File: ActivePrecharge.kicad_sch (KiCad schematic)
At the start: 34 parts, among them Con1 LED, J1 Conn_01x03, J2 Conn_01x02, J3 Conn_01x02, Q1 IRLML0030, U1 NCP785AH50T1G, U2 NCP785AH50T1G, U3 TLV9301xDCK, U4 TCMT1106

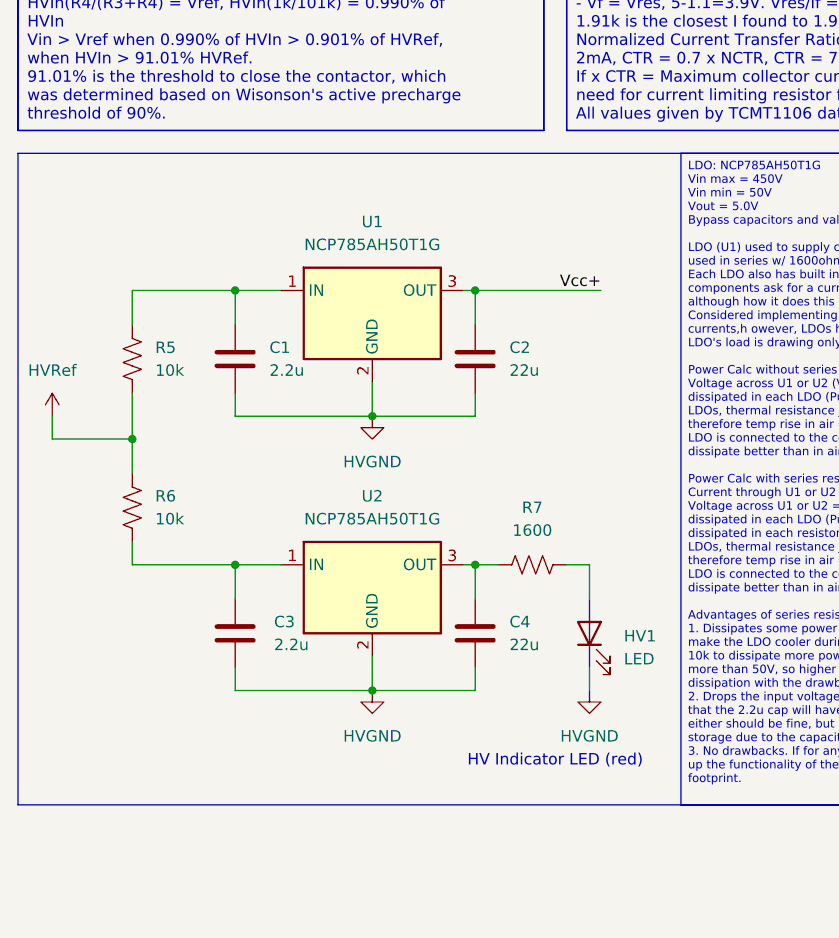
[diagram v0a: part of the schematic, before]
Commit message: 11/2 fixed incorrect footprint and symbol
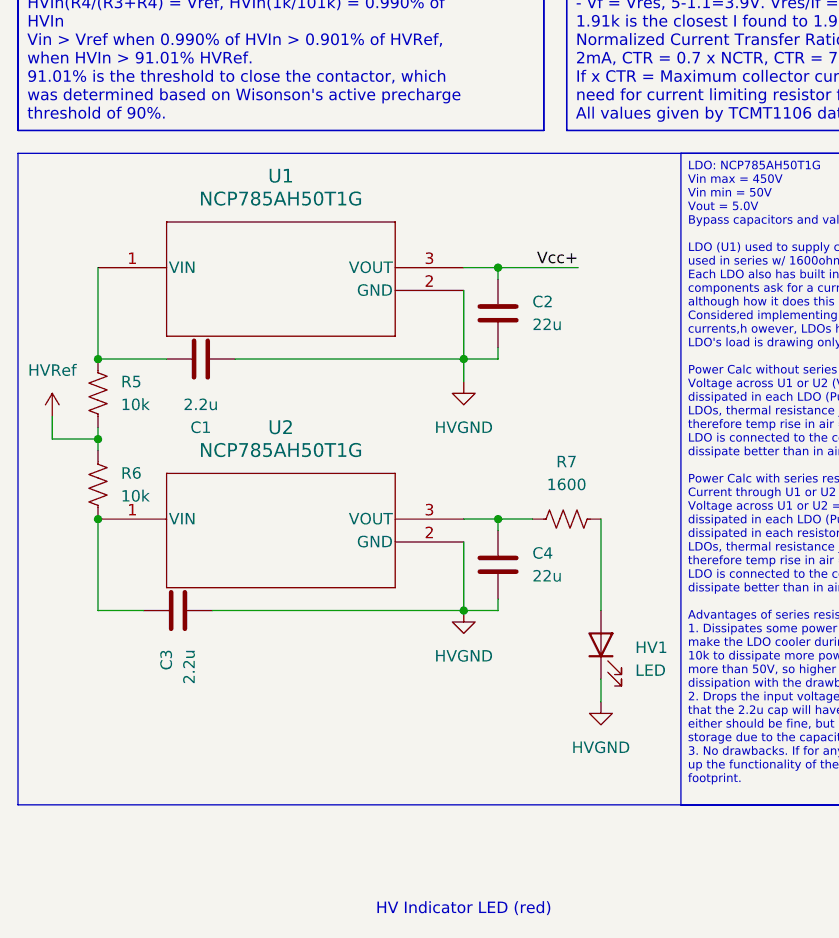
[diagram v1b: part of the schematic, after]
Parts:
- removed U1, U2: NCP785AH50T1G, Active-PrechargeLib:SOT-89-3_2P7X4P7_ONS, symbol Regulator_Linear:LT1963AxST-3.3
- added U1, U2: NCP785AH50T1G, Active-PrechargeLib:SOT-89-3_2P7X4P7_ONS, symbol NCP785:NCP785AH50T1G
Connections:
- net HVGND: now also C2.1, C4.1, U1.2 (GND), U2.2 (GND); no longer C2.2, C4.2
- net Vcc+: now also C2.2, U1.3 (VOUT); no longer C2.1
- net at C3.1, R6.1: now also U2.1 (VIN)
- net at R7.1: now also C4.2, U2.3 (VOUT); no longer C4.1
- net at C1.1, R5.2: now also U1.1 (VIN)
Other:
- moved on the sheet: C1, C2, C3, C4, HV1, R5, R6, R7

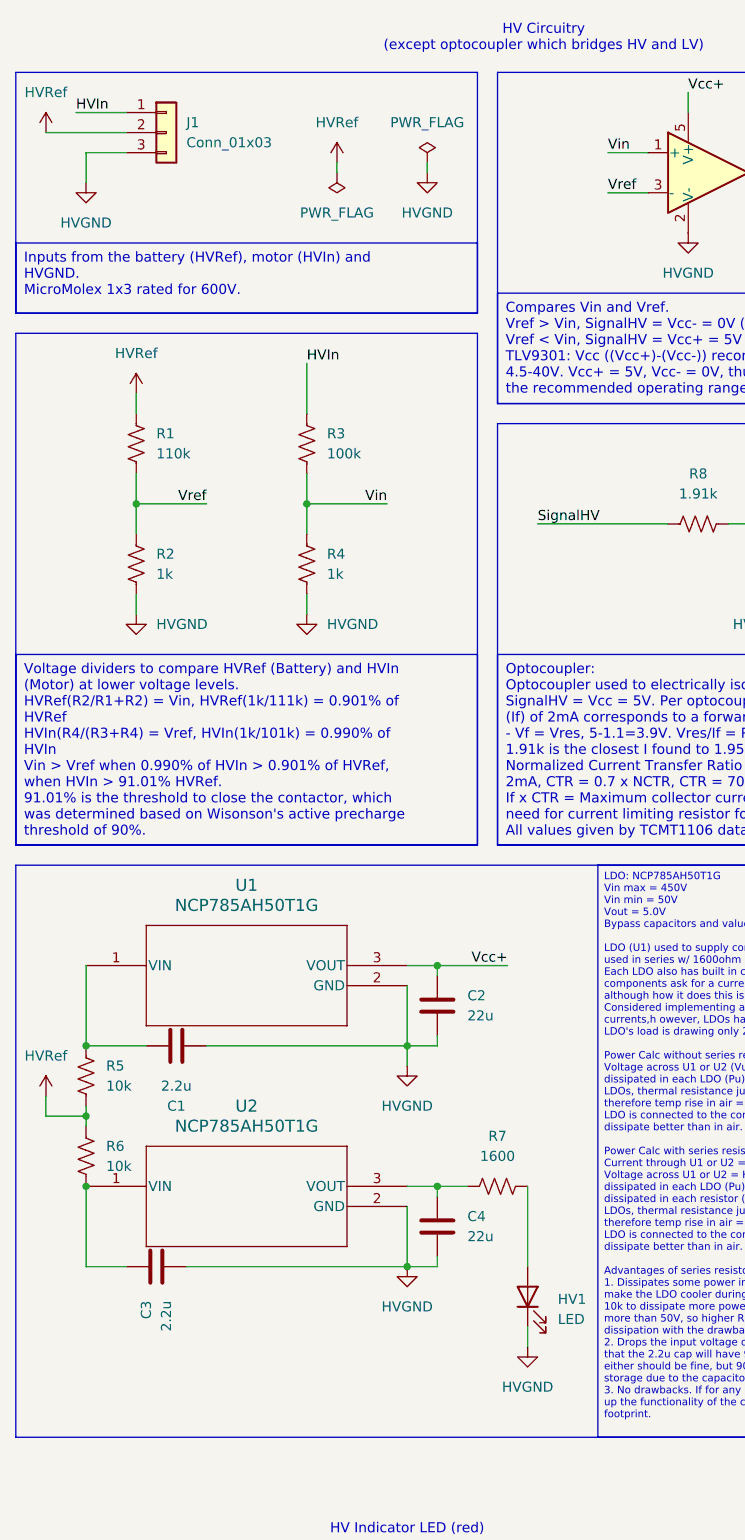
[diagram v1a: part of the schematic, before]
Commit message: adjusted HVGND position to be more centralized, added backplane traces and vias to route HVGND up to somewhat isolated top region, routed R1, R3 top plane traces on the back
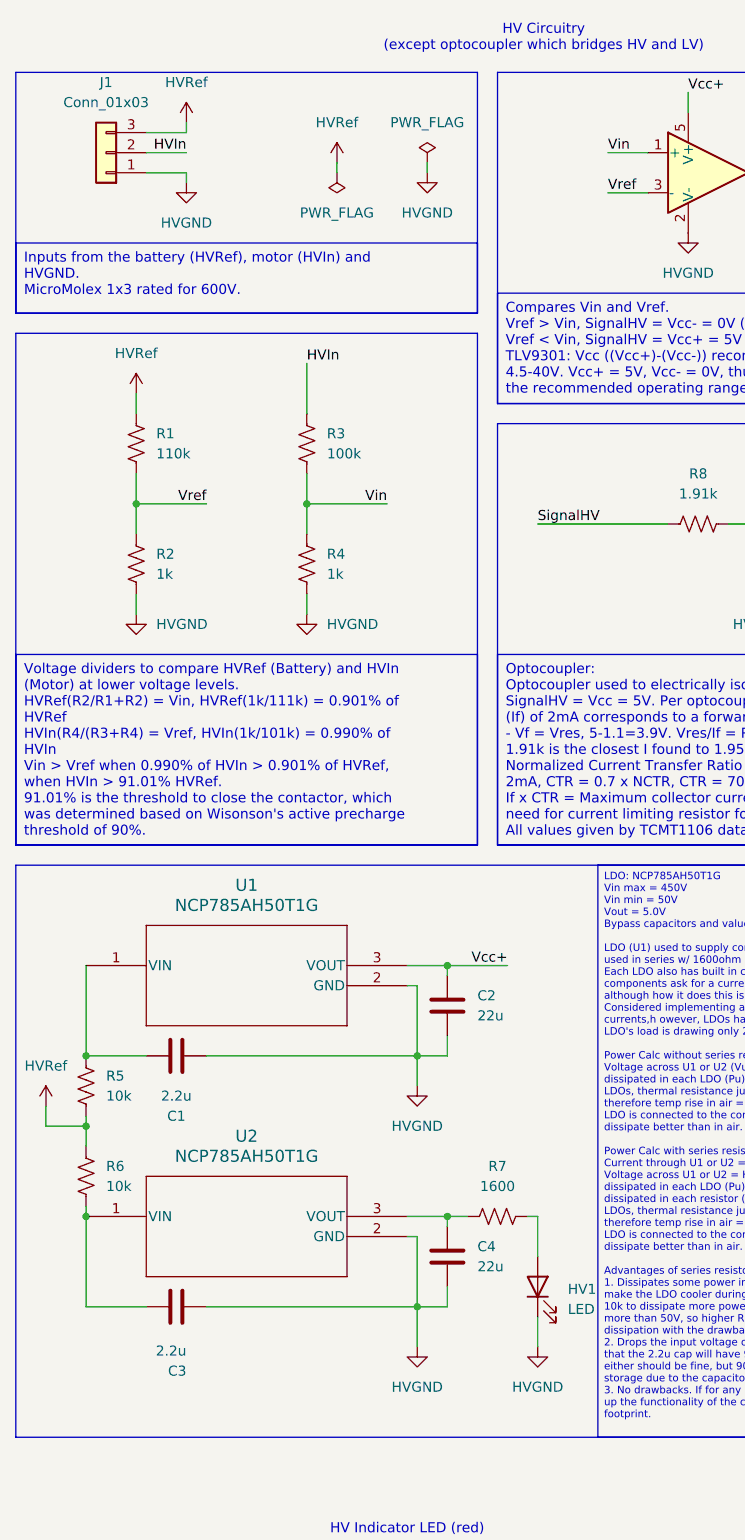
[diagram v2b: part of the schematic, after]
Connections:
- net HVGND: now also J1.1 (Pin_1); no longer J1.3 (Pin_3)
- net HVIn: now also J1.2 (Pin_2); no longer J1.1 (Pin_1)
- net HVRef: now also J1.3 (Pin_3); no longer J1.2 (Pin_2)
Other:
- moved on the sheet: C1, C2, C3, C4, HV1, J1, R5, R6, R7, U2

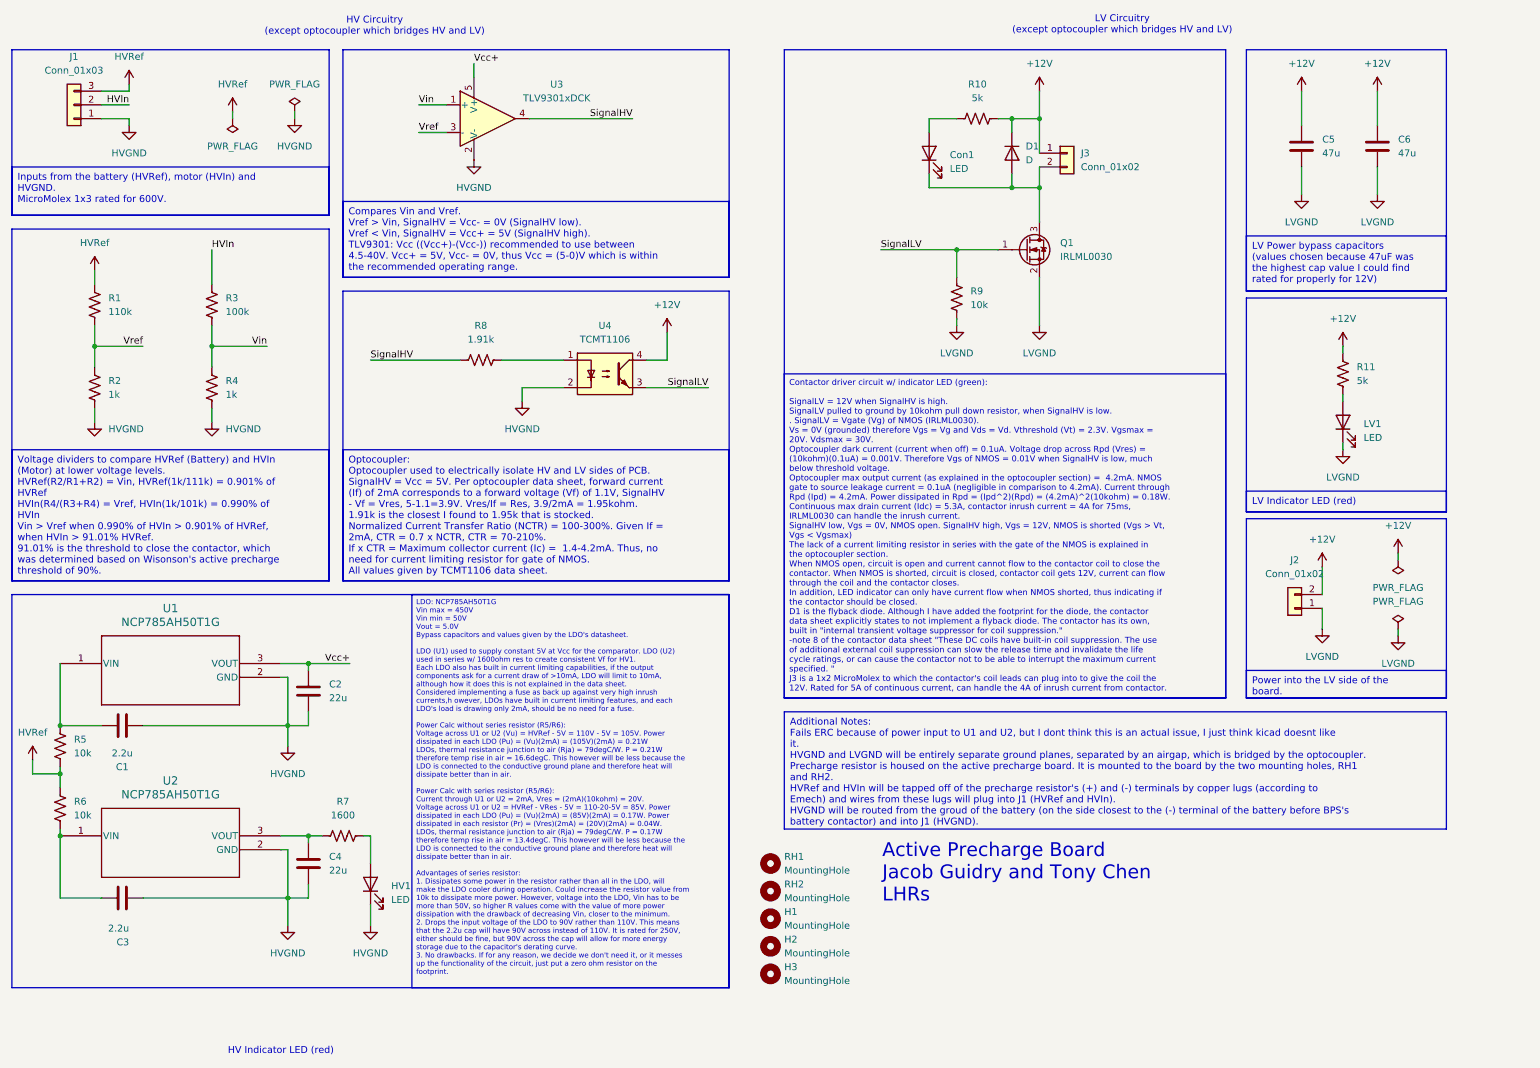
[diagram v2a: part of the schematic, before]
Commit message: initial sch and layout changes w/ test points
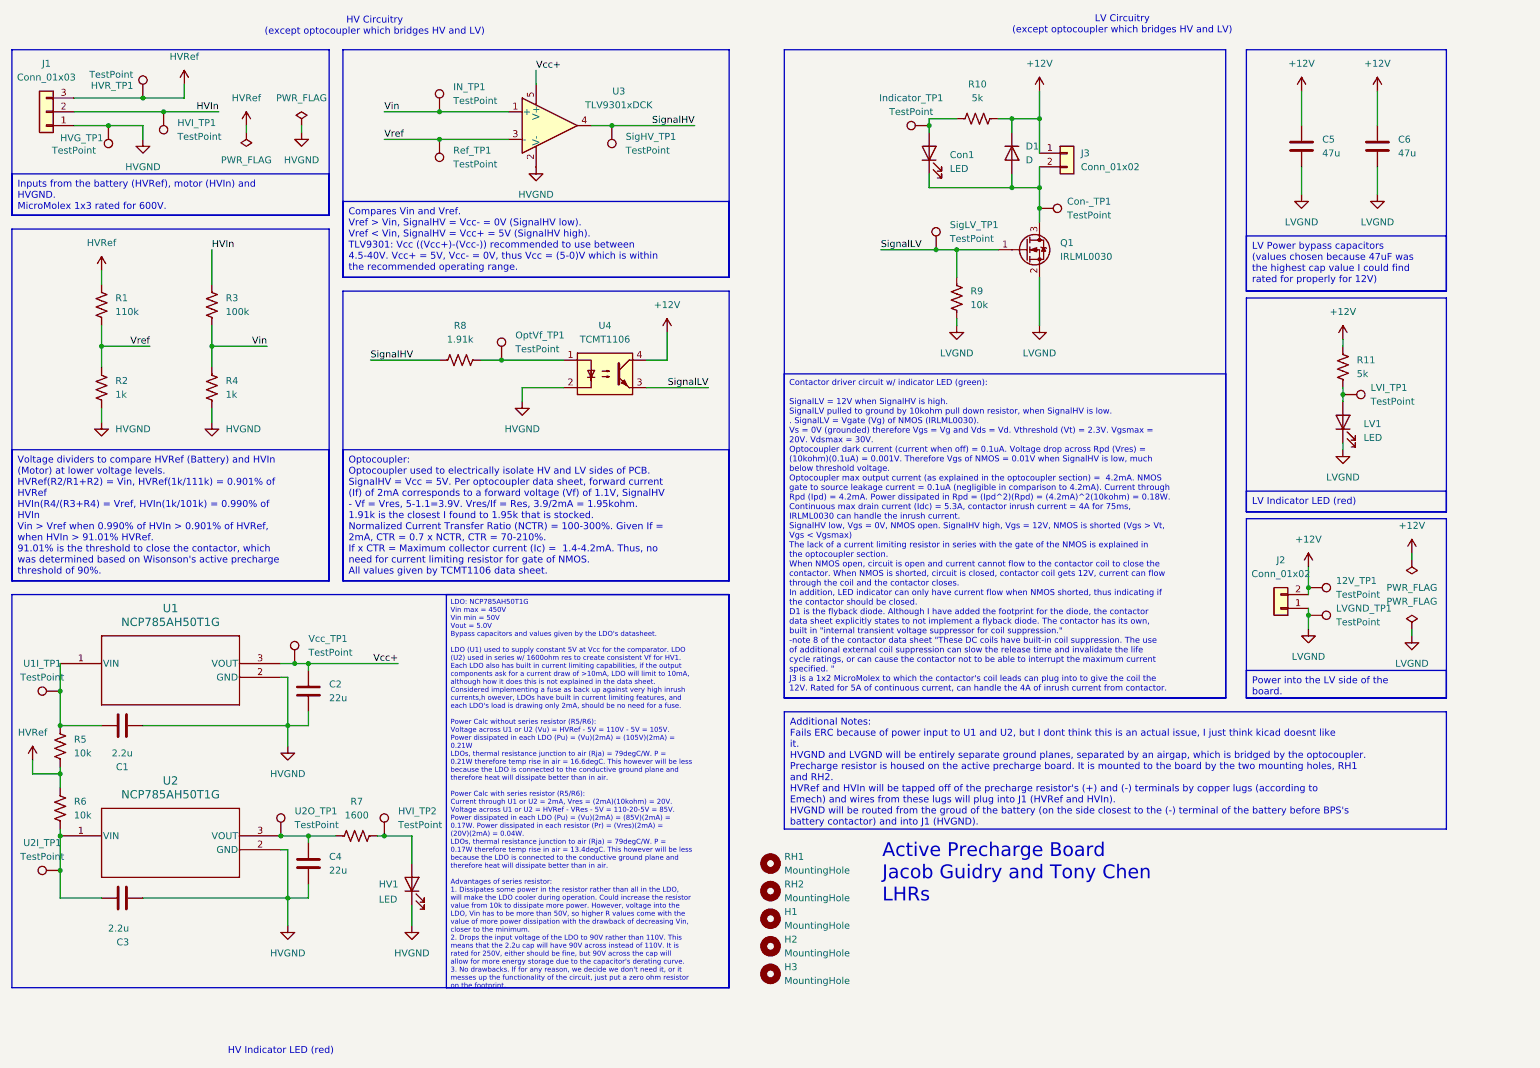
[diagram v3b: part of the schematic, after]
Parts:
- added 12V_TP1, Con-_TP1, HVG_TP1, HVI_TP1, HVI_TP2, HVR_TP1, IN_TP1, Indicator_TP1, LVGND_TP1, LVI_TP1, OptVf_TP1, Ref_TP1, SigHV_TP1, SigLV_TP1, U1I_TP1, U2I_TP1, U2O_TP1, Vcc_TP1: TestPoint, Active-PrechargeLib:TestPoint_HEX_3mmID, symbol Connector:TestPoint
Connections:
- net +12V: now also 12V_TP1.1
- net HVGND: now also HVG_TP1.1
- net HVIn: now also HVI_TP1.1
- net HVRef: now also HVR_TP1.1
- net LVGND: now also LVGND_TP1.1
- net SignalHV: now also SigHV_TP1.1
- net SignalLV: now also SigLV_TP1.1
- net Vcc+: now also Vcc_TP1.1
- net Vin: now also IN_TP1.1
- net Vref: now also Ref_TP1.1
- net at Con1.1 (K), D1.2 (A), J3.2 (Pin_2)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: now also Con-_TP1.1
- net at R8.2, U4.1: now also OptVf_TP1.1
- net at C1.1, R5.2, U1.1 (VIN): now also U1I_TP1.1
- net at HV1.2 (A), R7.2: now also HVI_TP2.1
- net at C3.1, R6.1, U2.1 (VIN): now also U2I_TP1.1
- net at C4.2, R7.1, U2.3 (VOUT): now also U2O_TP1.1
- net at LV1.2 (A), R11.2: now also LVI_TP1.1
- net at Con1.2 (A), R10.1: now also Indicator_TP1.1
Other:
- moved on the sheet: HV1, J1, J2, R1, R11, R2, R7, R8, U3
